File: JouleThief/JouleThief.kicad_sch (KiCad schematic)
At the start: 11 parts, among them J1 Screw_Terminal_01x02, J2 Screw_Terminal_01x02, Q1 BC547, Q2 BC547

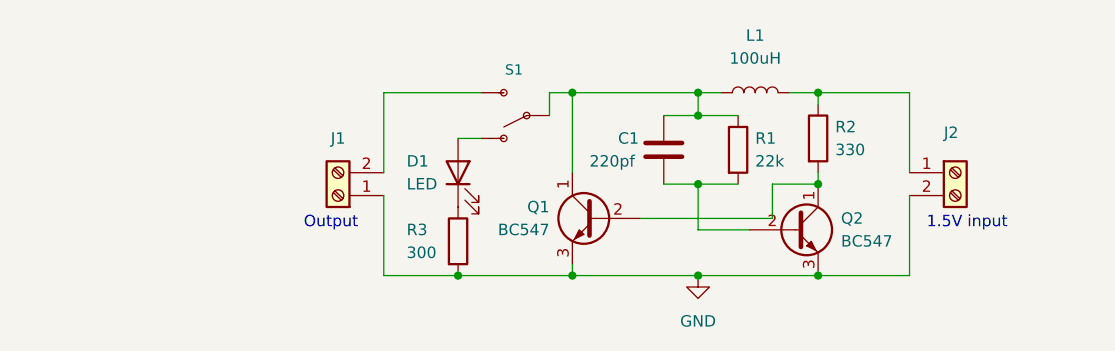
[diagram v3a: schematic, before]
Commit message: Finished SMD JouleThief functional
added silkscreen
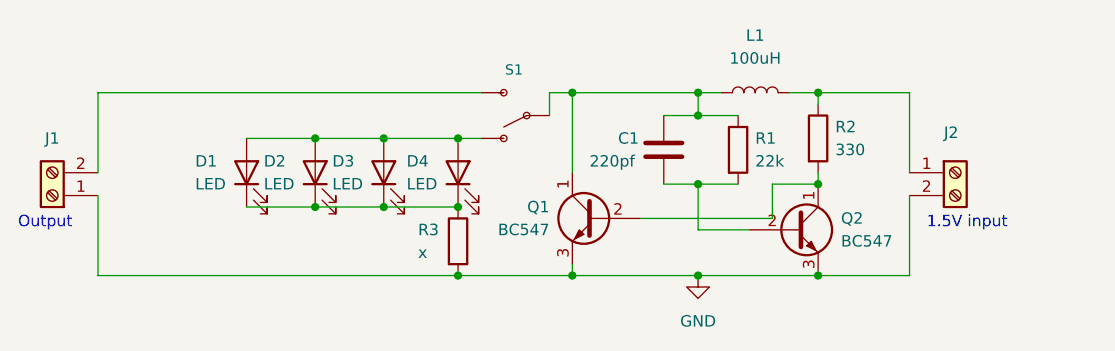
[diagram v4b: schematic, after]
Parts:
- added D1, D2, D3: LED, LED_SMD:LED_0805_2012Metric_Pad1.15x1.40mm_HandSolder, symbol Device:LED
- R3: value 300 -> x
- renumbered D1 to D4
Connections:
- net at D4.2 (A), S1.1 (O): now also D1.2 (A), D2.2 (A), D3.2 (A)
- net at D4.1 (K), R3.1: now also D1.1 (K), D2.1 (K), D3.1 (K)
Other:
- moved on the sheet: J1
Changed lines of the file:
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@@
   (junction (at 151.765 90.805) (diameter 0) (color 0 0 0 0)
   )
+  (junction (at 109.22 95.885) (diameter 0) (color 0 0 0 0)
+  )
   (junction (at 137.795 90.805) (diameter 0) (color 0 0 0 0)
   )
   (junction (at 151.765 100.965) (diameter 0) (color 0 0 0 0)
   )
+  (junction (at 109.22 103.505) (diameter 0) (color 0 0 0 0)
+  )
   (junction (at 165.1 100.965) (diameter 0) (color 0 0 0 0)
   )
+  (junction (at 116.84 103.505) (diameter 0) (color 0 0 0 0)
+  )
   (junction (at 151.765 111.125) (diameter 0) (color 0 0 0 0)
   )
+  (junction (at 125.095 95.885) (diameter 0) (color 0 0 0 0)
+  )
+  (junction (at 116.84 95.885) (diameter 0) (color 0 0 0 0)
+  )
   (junction (at 125.095 111.125) (diameter 0) (color 0 0 0 0)
   )
@@
   (junction (at 165.1 111.125) (diameter 0) (color 0 0 0 0)
   )
+  (junction (at 125.095 103.505) (diameter 0) (color 0 0 0 0)
+  )
   (junction (at 165.1 90.805) (diameter 0) (color 0 0 0 0)
   )
   (junction (at 137.795 111.125) (diameter 0) (color 0 0 0 0)
   )
-  (wire (pts (xy 116.84 111.125) (xy 125.095 111.125))
+  (wire (pts (xy 85.09 111.125) (xy 125.095 111.125))
+    (stroke (width 0) (type default) (color 0 0 0 0))
+  )
+  (wire (pts (xy 109.22 103.505) (xy 116.84 103.505))
     (stroke (width 0) (type default) (color 0 0 0 0))
   )
@@
     (stroke (width 0) (type default) (color 0 0 0 0))
   )
+  (wire (pts (xy 116.84 103.505) (xy 125.095 103.505))
+    (stroke (width 0) (type default) (color 0 0 0 0))
+  )
   (wire (pts (xy 147.955 100.965) (xy 151.765 100.965))
     (stroke (width 0) (type default) (color 0 0 0 0))
@@
     (stroke (width 0) (type default) (color 0 0 0 0))
   )
+  (wire (pts (xy 116.84 95.885) (xy 125.095 95.885))
+    (stroke (width 0) (type default) (color 0 0 0 0))
+  )
   (wire (pts (xy 156.21 93.345) (xy 151.765 93.345))
     (stroke (width 0) (type default) (color 0 0 0 0))
@@
     (stroke (width 0) (type default) (color 0 0 0 0))
   )
-  (wire (pts (xy 116.84 111.125) (xy 116.84 102.235))
+  (wire (pts (xy 85.09 111.125) (xy 85.09 102.235))
     (stroke (width 0) (type default) (color 0 0 0 0))
   )
@@
     (stroke (width 0) (type default) (color 0 0 0 0))
   )
+  (wire (pts (xy 101.6 103.505) (xy 109.22 103.505))
+    (stroke (width 0) (type default) (color 0 0 0 0))
+  )
   (wire (pts (xy 151.765 100.965) (xy 156.21 100.965))
     (stroke (width 0) (type default) (color 0 0 0 0))
@@
     (stroke (width 0) (type default) (color 0 0 0 0))
   )
+  (wire (pts (xy 101.6 95.885) (xy 109.22 95.885))
+    (stroke (width 0) (type default) (color 0 0 0 0))
+  )
   (wire (pts (xy 175.26 90.805) (xy 165.1 90.805))
     (stroke (width 0) (type default) (color 0 0 0 0))
@@
     (stroke (width 0) (type default) (color 0 0 0 0))
   )
-  (wire (pts (xy 116.84 99.695) (xy 116.84 90.805))
-    (stroke (width 0) (type default) (color 0 0 0 0))
-  )
-  (wire (pts (xy 116.84 90.805) (xy 127.635 90.805))
+  (wire (pts (xy 85.09 99.695) (xy 85.09 90.805))
+    (stroke (width 0) (type default) (color 0 0 0 0))
+  )
+  (wire (pts (xy 85.09 90.805) (xy 127.635 90.805))
     (stroke (width 0) (type default) (color 0 0 0 0))
   )
   (wire (pts (xy 135.255 93.345) (xy 135.255 90.805))
+    (stroke (width 0) (type default) (color 0 0 0 0))
+  )
+  (wire (pts (xy 109.22 95.885) (xy 116.84 95.885))
     (stroke (width 0) (type default) (color 0 0 0 0))
   )
@@
     (effects (font (size 1.27 1.27)) (justify left bottom))
   )
-  (text "Output" (at 107.95 106.045 0)
+  (text "Output" (at 76.2 106.045 0)
     (effects (font (size 1.27 1.27)) (justify left bottom))
   )
@@
     )
     (property "Datasheet" "~" (id 3) (at 180.34 99.695 0)
+      (effects (font (size 1.27 1.27)) hide)
+    )
+    (pin "1")
+    (pin "2")
+  )
+  (symbol (lib_id "Device:LED") (at 116.84 99.695 90) (unit 1)
+    (in_bom yes) (on_board yes)
+    (property "Reference" "D3" (id 0) (at 111.125 98.425 90)
+      (effects (font (size 1.27 1.27)) (justify right))
+    )
+    (property "Value" "LED" (id 1) (at 111.125 100.965 90)
+      (effects (font (size 1.27 1.27)) (justify right))
+    )
+    (property "Footprint" "LED_SMD:LED_0805_2012Metric_Pad1.15x1.40mm_HandSolder" (id 2) (at 116.84 99.695 0)
+      (effects (font (size 1.27 1.27)) hide)
+    )
+    (property "Datasheet" "~" (id 3) (at 116.84 99.695 0)
       (effects (font (size 1.27 1.27)) hide)
     )
@@
     (pin "1")
   )
-  (symbol (lib_id "Connector:Screw_Terminal_01x02") (at 111.76 102.235 180) (unit 1)
+  (symbol (lib_id "Device:LED") (at 101.6 99.695 90) (unit 1)
+    (in_bom yes) (on_board yes)
+    (property "Reference" "D1" (id 0) (at 95.885 98.425 90)
+      (effects (font (size 1.27 1.27)) (justify right))
+    )
+    (property "Value" "LED" (id 1) (at 95.885 100.965 90)
+      (effects (font (size 1.27 1.27)) (justify right))
+    )
+    (property "Footprint" "LED_SMD:LED_0805_2012Metric_Pad1.15x1.40mm_HandSolder" (id 2) (at 101.6 99.695 0)
+      (effects (font (size 1.27 1.27)) hide)
+    )
+    (property "Datasheet" "~" (id 3) (at 101.6 99.695 0)
+      (effects (font (size 1.27 1.27)) hide)
+    )
+    (pin "1")
+    (pin "2")
+  )
+  (symbol (lib_id "Connector:Screw_Terminal_01x02") (at 80.01 102.235 180) (unit 1)
     (in_bom yes) (on_board yes) (fields_autoplaced)
-    (property "Reference" "J1" (id 0) (at 111.76 95.885 0))
-    (property "Value" "Screw_Terminal_01x02" (id 1) (at 111.76 95.25 0)
-      (effects (font (size 1.27 1.27)) hide)
-    )
-    (property "Footprint" "TerminalBlock:TerminalBlock_bornier-2_P5.08mm" (id 2) (at 111.76 102.235 0)
-      (effects (font (size 1.27 1.27)) hide)
-    )
-    (property "Datasheet" "~" (id 3) (at 111.76 102.235 0)
+    (property "Reference" "J1" (id 0) (at 80.01 95.885 0))
+    (property "Value" "Screw_Terminal_01x02" (id 1) (at 80.01 95.25 0)
+      (effects (font (size 1.27 1.27)) hide)
+    )
+    (property "Footprint" "TerminalBlock:TerminalBlock_bornier-2_P5.08mm" (id 2) (at 80.01 102.235 0)
+      (effects (font (size 1.27 1.27)) hide)
+    )
+    (property "Datasheet" "~" (id 3) (at 80.01 102.235 0)
+      (effects (font (size 1.27 1.27)) hide)
+    )
+    (pin "1")
+    (pin "2")
+  )
+  (symbol (lib_id "Device:LED") (at 109.22 99.695 90) (unit 1)
+    (in_bom yes) (on_board yes)
+    (property "Reference" "D2" (id 0) (at 103.505 98.425 90)
+      (effects (font (size 1.27 1.27)) (justify right))
+    )
+    (property "Value" "LED" (id 1) (at 103.505 100.965 90)
+      (effects (font (size 1.27 1.27)) (justify right))
+    )
+    (property "Footprint" "LED_SMD:LED_0805_2012Metric_Pad1.15x1.40mm_HandSolder" (id 2) (at 109.22 99.695 0)
+      (effects (font (size 1.27 1.27)) hide)
+    )
+    (property "Datasheet" "~" (id 3) (at 109.22 99.695 0)
       (effects (font (size 1.27 1.27)) hide)
     )
@@
   (symbol (lib_id "Device:LED") (at 125.095 99.695 90) (unit 1)
     (in_bom yes) (on_board yes)
-    (property "Reference" "D1" (id 0) (at 119.38 98.425 90)
+    (property "Reference" "D4" (id 0) (at 119.38 98.425 90)
       (effects (font (size 1.27 1.27)) (justify right))
     )
@@
   (symbol (lib_id "Device:R") (at 125.095 107.315 0) (unit 1)
     (in_bom yes) (on_board yes)
-    (property "Reference" "R3" (id 0) (at 119.38 106.045 0)
-      (effects (font (size 1.27 1.27)) (justify left))
-    )
-    (property "Value" "300" (id 1) (at 119.38 108.585 0)
+    (property "Reference" "R3" (id 0) (at 120.65 106.045 0)
+      (effects (font (size 1.27 1.27)) (justify left))
+    )
+    (property "Value" "x" (id 1) (at 120.65 108.585 0)
       (effects (font (size 1.27 1.27)) (justify left))
     )
@@
       (reference "C1") (unit 1) (value "220pf") (footprint "Capacitor_SMD:C_0805_2012Metric_Pad1.18x1.45mm_HandSolder")
     )
+    (path "/a3379bb9-2fa5-4298-a436-0e0faa7bcb5e"
+      (reference "D1") (unit 1) (value "LED") (footprint "LED_SMD:LED_0805_2012Metric_Pad1.15x1.40mm_HandSolder")
+    )
+    (path "/d156950b-aa7e-4415-90f6-d17a4996de0e"
+      (reference "D2") (unit 1) (value "LED") (footprint "LED_SMD:LED_0805_2012Metric_Pad1.15x1.40mm_HandSolder")
+    )
+    (path "/2c5e3b91-00a4-441c-a5d0-5cef8c01ab08"
+      (reference "D3") (unit 1) (value "LED") (footprint "LED_SMD:LED_0805_2012Metric_Pad1.15x1.40mm_HandSolder")
+    )
     (path "/e027e40e-245b-4b6b-928b-0501a7da5de5"
-      (reference "D1") (unit 1) (value "LED") (footprint "LED_SMD:LED_0805_2012Metric_Pad1.15x1.40mm_HandSolder")
+      (reference "D4") (unit 1) (value "LED") (footprint "LED_SMD:LED_0805_2012Metric_Pad1.15x1.40mm_HandSolder")
     )
     (path "/c5208d8c-5be5-4514-b93e-909a9ac14ee6"
@@
     )
     (path "/fec27d13-0747-41e3-a4d8-e21a45052ada"
-      (reference "R3") (unit 1) (value "300") (footprint "Resistor_SMD:R_0805_2012Metric_Pad1.20x1.40mm_HandSolder")
+      (reference "R3") (unit 1) (value "x") (footprint "Resistor_SMD:R_0805_2012Metric_Pad1.20x1.40mm_HandSolder")
     )
     (path "/5a60103d-c1f5-44fb-9ca6-bd09329bef56"

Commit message: production and smooth traces add
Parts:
- R3: Purpose (none) -> led current resistor
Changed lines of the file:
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@@
+      (effects (font (size 1.27 1.27)) hide)
+    )
+    (property "Purpose" "led current resistor" (id 4) (at 125.095 107.315 0)
       (effects (font (size 1.27 1.27)) hide)
     )
